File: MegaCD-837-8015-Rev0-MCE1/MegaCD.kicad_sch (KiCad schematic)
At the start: 126 parts, among them CN1 CON 25P ANGLE, CN2 EDGE 60P, CN3 CON 21P, IC1 68HC000, IC10 MB8464A-10L, IC11 TC511664BZ, IC12 TC511664BZ, IC13 65256BLFP-10T, IC14 65256BLFP-10T, IC15 LC8951, IC16 74HC00, IC17 MB8464A-90L, IC18 MB8464A-90L, IC19 74HC112, IC2 315-5477, IC20 74HC245, IC3 315-5476, IC4 27C1024, IC5 MB81C4256Z, IC5678 HM514270, IC6 MB81C4256Z, IC7 MB81C4256Z, IC8 MB81C4256Z, IC9 MB3790, J2 2TS, J3 MH, J4 CAS0, M0 TestPoint, M1 TestPoint, M10 TestPoint, M11 TestPoint, M2 TestPoint, M3 TestPoint, M4 TestPoint, M5 TestPoint, M6 TestPoint, M7 TestPoint, M8 TestPoint, M9 TestPoint

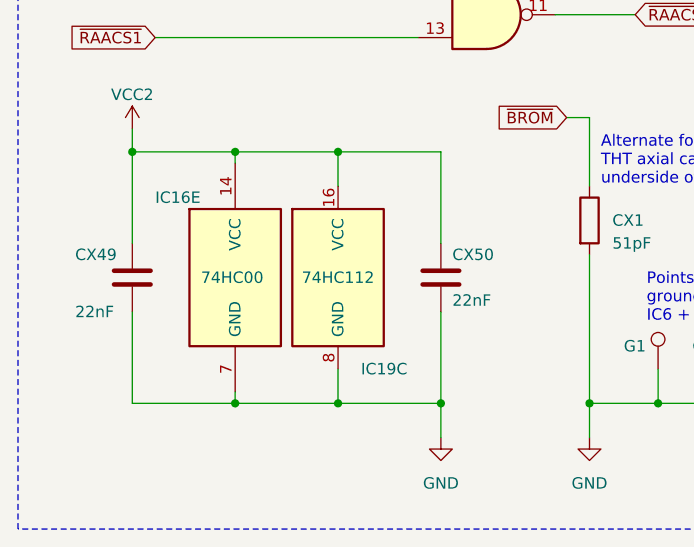
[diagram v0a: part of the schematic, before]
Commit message: Add 837-8952 Export board, minor updates for Japanese revisions (#1)
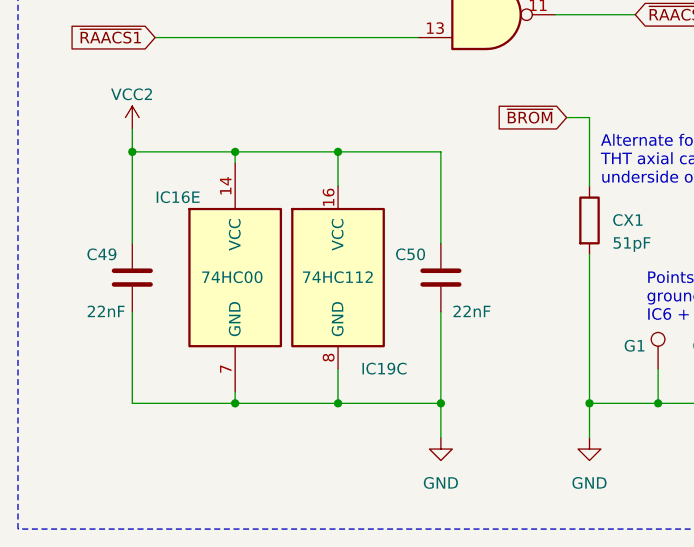
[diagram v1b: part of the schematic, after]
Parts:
- removed CX49, CX50: 22nF, MegaCD_Footprints:SMD_0805_HandSolder, symbol Device:C
- added C49, C50: 22nF, MegaCD_Footprints:SMD_0805_HandSolder_Medium, symbol Device:C
- C1, C14, C15, C16, C17, C18, C19, C2, C20, C21, C22, C24, C25, C27, C29, C3, C30, C32, C33, C34, C35, C36, C38, C39, C4, C40, C43, C44, C45, C47, C5, C51, C52, C54, C55, C5678, C6, C7, C8, CX1, CY49, CY50, R1, R2, R3, R4, R5, R6, R7: footprint MegaCD_Footprints:SMD_0805_HandSolder -> MegaCD_Footprints:SMD_0805_HandSolder_Medium
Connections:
- net GND: now also C49.2, C50.2
- net VCC2: now also C49.1, C50.1
